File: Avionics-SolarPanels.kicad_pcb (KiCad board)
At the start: 4 copper layers, 82 x 100 mm, 225 parts, among them J1 522711069, J2 522711069, Q1 MBT2222ADW1T1, Q10 NX3008NBKS, Q11 MBT2222ADW1T1, Q12 NX3008NBKS, Q13 IRLML2803, Q14 SIRA99DP-T1-GE3, Q15 SIRA99DP-T1-GE3, Q16 SIRA99DP-T1-GE3, Q17 SIRA99DP-T1-GE3, Q18 MBT2222ADW1T1, Q19 NX3008NBKS, Q2 NX3008NBKS, Q20 MBT2222ADW1T1, Q21 NX3008NBKS, Q3 MBT2222ADW1T1, Q4 NX3008NBKS, Q5 MBT2222ADW1T1, Q6 NX3008NBKS, Q7 MBT2222ADW1T1, Q8 NX3008NBKS, Q9 MBT2222ADW1T1, U1 OPT4003DNPRQ1, U10 D5V0P4UR6SO, U11 VL53L4CD, U2 ADM1176-1ARMZ-R7, U3 LTC4412xS6, U4 LTC4412xS6, U5 LTC4412xS6, U6 LTC3130IUDC, U7 LTC3130IUDC, U8 LTC3130IUDC, U9 DRV8235RTER

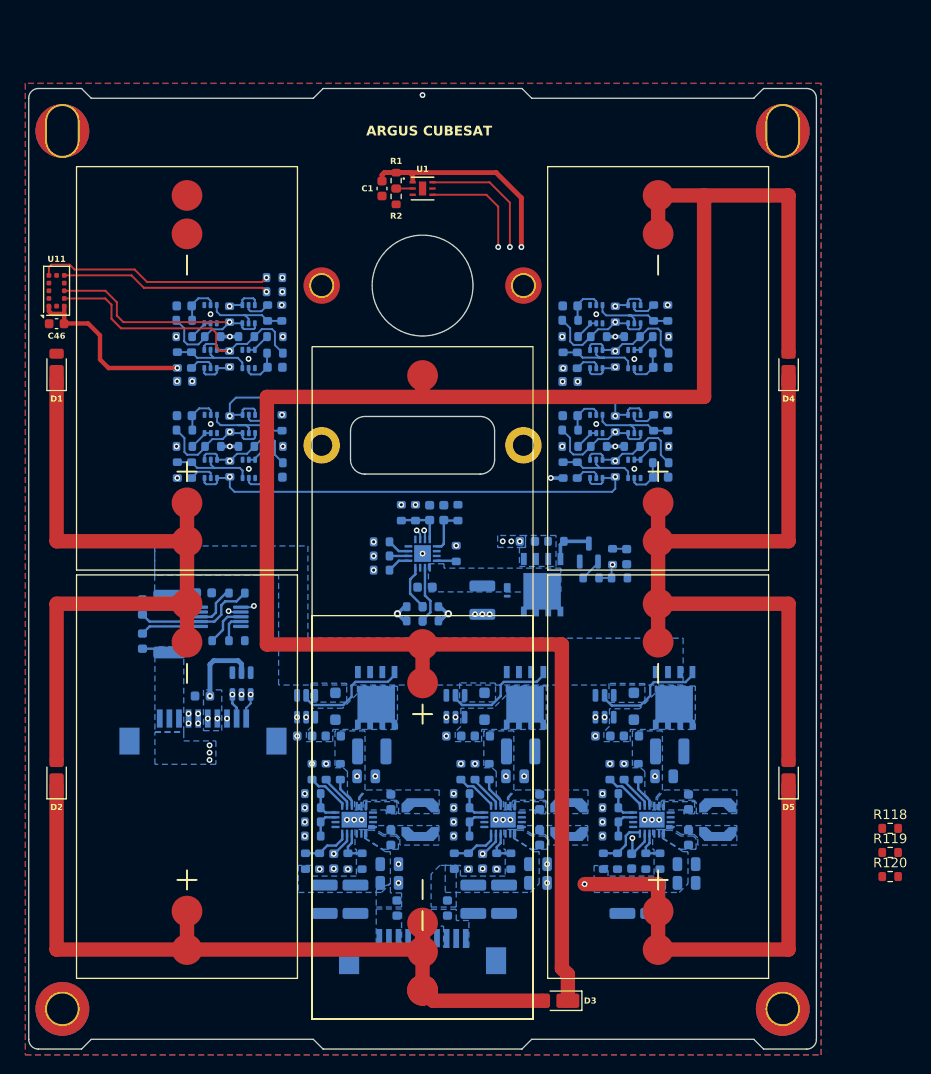
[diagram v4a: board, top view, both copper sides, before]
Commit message: V4 Updates and Cell Backer
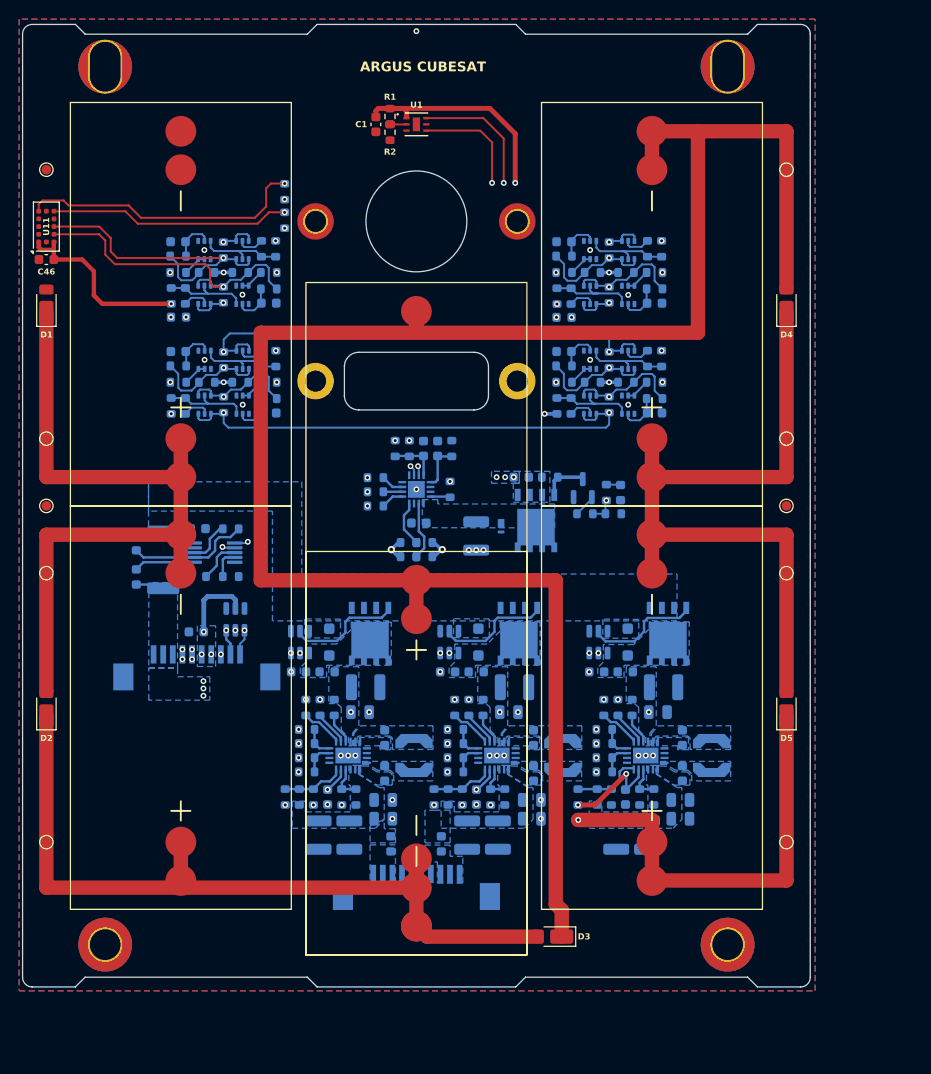
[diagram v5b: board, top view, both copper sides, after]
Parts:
- added H10: MountingHole_Pad, TestPoint:TestPoint_Pad_D1.0mm, F.Cu at (113.2, 130.9)
- added H11: MountingHole_Pad, TestPoint:TestPoint_Pad_D1.0mm, F.Cu at (190.3, 60.9)
- added H12: MountingHole_Pad, TestPoint:TestPoint_Pad_D1.0mm, F.Cu at (190.3, 88.9)
- added H13: MountingHole_Pad, TestPoint:TestPoint_Pad_D1.0mm, F.Cu at (113.2, 102.9)
- added H14: MountingHole_Pad, TestPoint:TestPoint_Pad_D1.0mm, F.Cu at (190.3, 102.9)
- added H15: MountingHole_Pad, TestPoint:TestPoint_Pad_D1.0mm, F.Cu at (113.2, 95.9)
- added H16: MountingHole_Pad, TestPoint:TestPoint_Pad_D1.0mm, F.Cu at (190.3, 95.9)
- added H19: MountingHole_Pad, TestPoint:TestPoint_Pad_D1.0mm, F.Cu at (190.3, 130.9)
- added H8: MountingHole_Pad, TestPoint:TestPoint_Pad_D1.0mm, F.Cu at (113.2, 60.9)
- added H9: MountingHole_Pad, TestPoint:TestPoint_Pad_D1.0mm, F.Cu at (113.2, 88.9)
- R1, R2: value ?R -> 0R
- R118, R119, R120: moved to B.Cu
- moved R119 63.2 mm to (138.1, 126.2), turned to 90 degrees
- moved R118 47.6 mm to (153.6, 126.2), turned to 90 degrees
- moved R120 33.5 mm to (168.6, 126.2), turned to 90 degrees
- moved R104 9.00 mm to (138.0, 63.1), turned to 90 degrees
- moved H2 8.81 mm to (184.2, 141.5)
- moved H1 8.81 mm to (184.2, 50.1)
- moved H4 8.04 mm to (119.4, 50.1)
- moved H3 8.04 mm to (119.4, 141.5)
- moved R103 7.52 mm to (138.0, 66.1), turned to 90 degrees
- moved D2 7.27 mm to (113.2, 116.9)
- moved SC2 7.22 mm to (127.2, 116.9)
- moved SC5 7.22 mm to (176.3, 116.9)
- moved D5 7.19 mm to (190.3, 116.9)
- moved C46 6.76 mm to (113.2, 70.2)
- moved D1 6.76 mm to (113.2, 74.9)
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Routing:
- net /Solar Charger/MPPT/VCC: track 8.62 -> 15.6 mm, vias 2 -> 3
- net /Solar Charger/MPPT1/VCC: track 8.65 -> 14.4 mm, vias 2 -> 3
- net /Solar Charger/MPPT2/VCC: track 8.67 -> 14.4 mm, vias 2 -> 3
- net Net-(U11-XSHUT): track 24.6 -> 29.8 mm
- net Net-(U11-GPIO1): track 21.8 -> 25.0 mm
- net /Coil Driver/coil: track 14493.1 -> 14495.9 mm
- net /Solar Charger/MPPC: track 5.25 -> 7.79 mm
- net /Light Sensor/LS_3V3: track 34.3 -> 32.7 mm
- net Net-(D2-K): track 81.8 -> 83.3 mm
- net /Solar Charger/MPPC2: track 5.02 -> 6.49 mm
- net /Solar Charger/MPPC1: track 5.08 -> 6.55 mm
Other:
- board size 82 x 100 mm -> 82 x 100.2 mm
- board text added: "ARGUS Cubesat Carnegie Mellon University X/Y Solar Panel v4.0"
- board text removed: "ARGUS Cubesat Carnegie Mellon University X/Y Solar Panel v3.1"
